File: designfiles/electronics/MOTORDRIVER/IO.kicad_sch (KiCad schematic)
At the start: 17 parts, among them J1 IMU1, J2 IMU2, J3 Conn_01x04_Socket, J4 Screw_Terminal_01x02, P1 USB_C_Plug_USB2.0, SW1 SW_DPST_x2

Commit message: made clearer foldernames and cleaned up
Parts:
- renumbered R115 to R42, R113 to R43
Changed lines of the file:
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@@
 		(dnp no)
 		(fields_autoplaced yes)
-		(property "Reference" "#PWR0330"
+		(property "Reference" "#PWR060"
 			(at 34.29 107.95 0)
 			(effects
@@
 			(project "motordriver"
 				(path "/c7634e88-16d1-45ec-9aac-9c841e03cf6d/38bc72d2-c2f6-4538-9c33-e1ab2a8ac987"
-					(reference "#PWR0330")
+					(reference "#PWR060")
 					(unit 1)
 				)
@@
 		(dnp no)
 		(fields_autoplaced yes)
-		(property "Reference" "#PWR065"
+		(property "Reference" "#PWR069"
 			(at 139.7 92.71 0)
 			(effects
@@
 			(project "motordriver"
 				(path "/c7634e88-16d1-45ec-9aac-9c841e03cf6d/38bc72d2-c2f6-4538-9c33-e1ab2a8ac987"
-					(reference "#PWR065")
+					(reference "#PWR069")
 					(unit 1)
 				)
@@
 		(dnp no)
 		(fields_autoplaced yes)
-		(property "Reference" "#PWR058"
+		(property "Reference" "#PWR062"
 			(at 72.39 102.87 0)
 			(effects
@@
 			(project "motordriver"
 				(path "/c7634e88-16d1-45ec-9aac-9c841e03cf6d/38bc72d2-c2f6-4538-9c33-e1ab2a8ac987"
-					(reference "#PWR058")
+					(reference "#PWR062")
 					(unit 1)
 				)
@@
 		(dnp no)
 		(fields_autoplaced yes)
-		(property "Reference" "#PWR0333"
+		(property "Reference" "#PWR063"
 			(at 81.28 99.06 0)
 			(effects
@@
 			(project "motordriver"
 				(path "/c7634e88-16d1-45ec-9aac-9c841e03cf6d/38bc72d2-c2f6-4538-9c33-e1ab2a8ac987"
-					(reference "#PWR0333")
+					(reference "#PWR063")
 					(unit 1)
 				)
@@
 		(dnp no)
 		(fields_autoplaced yes)
-		(property "Reference" "#PWR064"
+		(property "Reference" "#PWR068"
 			(at 149.86 90.17 0)
 			(effects
@@
 			(project "motordriver"
 				(path "/c7634e88-16d1-45ec-9aac-9c841e03cf6d/38bc72d2-c2f6-4538-9c33-e1ab2a8ac987"
-					(reference "#PWR064")
+					(reference "#PWR068")
 					(unit 1)
 				)
@@
 		(dnp no)
 		(fields_autoplaced yes)
-		(property "Reference" "#PWR067"
+		(property "Reference" "#PWR071"
 			(at 139.7 106.68 0)
 			(effects
@@
 			(project "motordriver"
 				(path "/c7634e88-16d1-45ec-9aac-9c841e03cf6d/38bc72d2-c2f6-4538-9c33-e1ab2a8ac987"
-					(reference "#PWR067")
+					(reference "#PWR071")
 					(unit 1)
 				)
@@
 		(on_board yes)
 		(dnp no)
-		(property "Reference" "#PWR062"
+		(property "Reference" "#PWR066"
 			(at 121.92 113.03 0)
 			(effects
@@
 			(project "motordriver"
 				(path "/c7634e88-16d1-45ec-9aac-9c841e03cf6d/38bc72d2-c2f6-4538-9c33-e1ab2a8ac987"
-					(reference "#PWR062")
+					(reference "#PWR066")
 					(unit 1)
 				)
@@
 		(dnp no)
 		(fields_autoplaced yes)
-		(property "Reference" "#PWR072"
+		(property "Reference" "#PWR076"
 			(at 193.04 128.27 0)
 			(effects
@@
 			(project "motordriver"
 				(path "/c7634e88-16d1-45ec-9aac-9c841e03cf6d/38bc72d2-c2f6-4538-9c33-e1ab2a8ac987"
-					(reference "#PWR072")
+					(reference "#PWR076")
 					(unit 1)
 				)
@@
 		(dnp no)
 		(fields_autoplaced yes)
-		(property "Reference" "#PWR071"
+		(property "Reference" "#PWR075"
 			(at 190.5 99.06 0)
 			(effects
@@
 			(project "motordriver"
 				(path "/c7634e88-16d1-45ec-9aac-9c841e03cf6d/38bc72d2-c2f6-4538-9c33-e1ab2a8ac987"
-					(reference "#PWR071")
+					(reference "#PWR075")
 					(unit 1)
 				)
@@
 		(dnp no)
 		(fields_autoplaced yes)
-		(property "Reference" "#PWR068"
+		(property "Reference" "#PWR072"
 			(at 149.86 118.11 0)
 			(effects
@@
 			(project "motordriver"
 				(path "/c7634e88-16d1-45ec-9aac-9c841e03cf6d/38bc72d2-c2f6-4538-9c33-e1ab2a8ac987"
-					(reference "#PWR068")
+					(reference "#PWR072")
 					(unit 1)
 				)
@@
 		(dnp no)
 		(fields_autoplaced yes)
-		(property "Reference" "#PWR069"
+		(property "Reference" "#PWR073"
 			(at 139.7 120.65 0)
 			(effects
@@
 			(project "motordriver"
 				(path "/c7634e88-16d1-45ec-9aac-9c841e03cf6d/38bc72d2-c2f6-4538-9c33-e1ab2a8ac987"
-					(reference "#PWR069")
+					(reference "#PWR073")
 					(unit 1)
 				)
@@
 		(dnp no)
 		(fields_autoplaced yes)
-		(property "Reference" "#PWR066"
+		(property "Reference" "#PWR070"
 			(at 149.86 104.14 0)
 			(effects
@@
 			(project "motordriver"
 				(path "/c7634e88-16d1-45ec-9aac-9c841e03cf6d/38bc72d2-c2f6-4538-9c33-e1ab2a8ac987"
-					(reference "#PWR066")
+					(reference "#PWR070")
 					(unit 1)
 				)
@@
 		(dnp no)
 		(fields_autoplaced yes)
-		(property "Reference" "R113"
+		(property "Reference" "R43"
 			(at 76.2 83.82 90)
 			(effects
@@
 			(project "motordriver"
 				(path "/c7634e88-16d1-45ec-9aac-9c841e03cf6d/38bc72d2-c2f6-4538-9c33-e1ab2a8ac987"
-					(reference "R113")
+					(reference "R43")
 					(unit 1)
 				)
@@
 		(dnp no)
 		(fields_autoplaced yes)
-		(property "Reference" "#PWR073"
+		(property "Reference" "#PWR078"
 			(at 242.57 96.52 0)
 			(effects
@@
 			(project "motordriver"
 				(path "/c7634e88-16d1-45ec-9aac-9c841e03cf6d/38bc72d2-c2f6-4538-9c33-e1ab2a8ac987"
-					(reference "#PWR073")
+					(reference "#PWR078")
 					(unit 1)
 				)
@@
 		(dnp no)
 		(fields_autoplaced yes)
-		(property "Reference" "#PWR074"
+		(property "Reference" "#PWR077"
 			(at 238.76 129.54 0)
 			(effects
@@
 			(project "motordriver"
 				(path "/c7634e88-16d1-45ec-9aac-9c841e03cf6d/38bc72d2-c2f6-4538-9c33-e1ab2a8ac987"
-					(reference "#PWR074")
+					(reference "#PWR077")
 					(unit 1)
 				)
@@
 		(on_board yes)
 		(dnp no)
-		(property "Reference" "#PWR063"
+		(property "Reference" "#PWR067"
 			(at 111.76 115.57 0)
 			(effects
@@
 			(project "motordriver"
 				(path "/c7634e88-16d1-45ec-9aac-9c841e03cf6d/38bc72d2-c2f6-4538-9c33-e1ab2a8ac987"
-					(reference "#PWR063")
+					(reference "#PWR067")
 					(unit 1)
 				)
@@
 		(dnp no)
 		(fields_autoplaced yes)
-		(property "Reference" "R115"
+		(property "Reference" "R42"
 			(at 27.94 88.9 90)
 			(effects
@@
 			(project "motordriver"
 				(path "/c7634e88-16d1-45ec-9aac-9c841e03cf6d/38bc72d2-c2f6-4538-9c33-e1ab2a8ac987"
-					(reference "R115")
+					(reference "R42")
 					(unit 1)
 				)
@@
 		(on_board yes)
 		(dnp no)
-		(property "Reference" "#PWR060"
+		(property "Reference" "#PWR064"
 			(at 121.92 86.36 0)
 			(effects
@@
 			(project "motordriver"
 				(path "/c7634e88-16d1-45ec-9aac-9c841e03cf6d/38bc72d2-c2f6-4538-9c33-e1ab2a8ac987"
-					(reference "#PWR060")
+					(reference "#PWR064")
 					(unit 1)
 				)
@@
 		(dnp no)
 		(fields_autoplaced yes)
-		(property "Reference" "#PWR0331"
+		(property "Reference" "#PWR061"
 			(at 34.29 110.49 0)
 			(effects
@@
 			(project "motordriver"
 				(path "/c7634e88-16d1-45ec-9aac-9c841e03cf6d/38bc72d2-c2f6-4538-9c33-e1ab2a8ac987"
-					(reference "#PWR0331")
+					(reference "#PWR061")
 					(unit 1)
 				)
@@
 		(dnp no)
 		(fields_autoplaced yes)
-		(property "Reference" "#PWR070"
+		(property "Reference" "#PWR074"
 			(at 176.53 93.98 0)
 			(effects
@@
 			(project "motordriver"
 				(path "/c7634e88-16d1-45ec-9aac-9c841e03cf6d/38bc72d2-c2f6-4538-9c33-e1ab2a8ac987"
-					(reference "#PWR070")
+					(reference "#PWR074")
 					(unit 1)
 				)
@@
 		(dnp no)
 		(fields_autoplaced yes)
-		(property "Reference" "#PWR0332"
+		(property "Reference" "#PWR058"
 			(at 22.86 104.14 0)
 			(effects
@@
 			(project "motordriver"
 				(path "/c7634e88-16d1-45ec-9aac-9c841e03cf6d/38bc72d2-c2f6-4538-9c33-e1ab2a8ac987"
-					(reference "#PWR0332")
+					(reference "#PWR058")
 					(unit 1)
 				)
@@
 		(on_board yes)
 		(dnp no)
-		(property "Reference" "#PWR061"
+		(property "Reference" "#PWR065"
 			(at 111.76 88.9 0)
 			(effects
@@
 			(project "motordriver"
 				(path "/c7634e88-16d1-45ec-9aac-9c841e03cf6d/38bc72d2-c2f6-4538-9c33-e1ab2a8ac987"
-					(reference "#PWR061")
-					(unit 1)
-				)
+					(reference "#PWR065")
+					(unit 1)
+				)

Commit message: removed backup files and found components for special resistors and diodes
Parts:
- renumbered R42 to R43, R43 to R44
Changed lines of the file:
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@@
 		(dnp no)
 		(fields_autoplaced yes)
-		(property "Reference" "R43"
+		(property "Reference" "R44"
 			(at 76.2 83.82 90)
 			(effects
@@
 			(project "motordriver"
 				(path "/c7634e88-16d1-45ec-9aac-9c841e03cf6d/38bc72d2-c2f6-4538-9c33-e1ab2a8ac987"
-					(reference "R43")
+					(reference "R44")
 					(unit 1)
 				)
@@
 		(dnp no)
 		(fields_autoplaced yes)
-		(property "Reference" "R42"
+		(property "Reference" "R43"
 			(at 27.94 88.9 90)
 			(effects
@@
 			(project "motordriver"
 				(path "/c7634e88-16d1-45ec-9aac-9c841e03cf6d/38bc72d2-c2f6-4538-9c33-e1ab2a8ac987"
-					(reference "R42")
-					(unit 1)
-				)
+					(reference "R43")
+					(unit 1)
+				)

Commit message: small tweaks
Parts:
- added SW1: SW_DPST_x2, Button_Switch_THT:SW_CK_JS202011AQN_DPDT_Angled, symbol Switch:SW_DPST_x2
- renumbered SW1 to SW2
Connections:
- new net RESETN: SW1.1 (A)
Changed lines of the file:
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@@
+		)
+	)
+	(hierarchical_label "RESETN"
+		(shape input)
+		(at 172.72 53.34 180)
+		(fields_autoplaced yes)
+		(effects
+			(font
+				(size 1.27 1.27)
+			)
+			(justify right)
 		)
 	)
@@
 	)
 	(symbol
+		(lib_id "Switch:SW_DPST_x2")
+		(at 177.8 53.34 0)
+		(unit 1)
+		(exclude_from_sim no)
+		(in_bom yes)
+		(on_board yes)
+		(dnp no)
+		(fields_autoplaced yes)
+		(property "Reference" "SW1"
+			(at 177.8 46.99 0)
+			(effects
+				(font
+					(size 1.27 1.27)
+				)
+			)
+		)
+		(property "Value" "SW_DPST_x2"
+			(at 177.8 49.53 0)
+			(effects
+				(font
+					(size 1.27 1.27)
+				)
+			)
+		)
+		(property "Footprint" "Button_Switch_THT:SW_CK_JS202011AQN_DPDT_Angled"
+			(at 177.8 53.34 0)
+			(effects
+				(font
+					(size 1.27 1.27)
+				)
+				(hide yes)
+			)
+		)
+		(property "Datasheet" "~"
+			(at 177.8 53.34 0)
+			(effects
+				(font
+					(size 1.27 1.27)
+				)
+				(hide yes)
+			)
+		)
+		(property "Description" "Single Pole Single Throw (SPST) switch, separate symbol"
+			(at 177.8 53.34 0)
+			(effects
+				(font
+					(size 1.27 1.27)
+				)
+				(hide yes)
+			)
+		)
+		(pin "3"
+		)
+		(pin "1"
+		)
+		(pin "4"
+		)
+		(pin "2"
+		)
+		(instances
+			(project "motordriver"
+				(path "/c7634e88-16d1-45ec-9aac-9c841e03cf6d/38bc72d2-c2f6-4538-9c33-e1ab2a8ac987"
+					(reference "SW1")
+					(unit 1)
+				)
+			)
+		)
+	)
+	(symbol
 		(lib_id "power:GND")
 		(at 81.28 92.71 0)
@@
 		(dnp no)
 		(fields_autoplaced yes)
-		(property "Reference" "SW1"
+		(property "Reference" "SW2"
 			(at 237.49 81.28 0)
 			(effects
@@
 			(project ""
 				(path "/c7634e88-16d1-45ec-9aac-9c841e03cf6d/38bc72d2-c2f6-4538-9c33-e1ab2a8ac987"
-					(reference "SW1")
-					(unit 1)
-				)
+					(reference "SW2")
+					(unit 1)
+				)

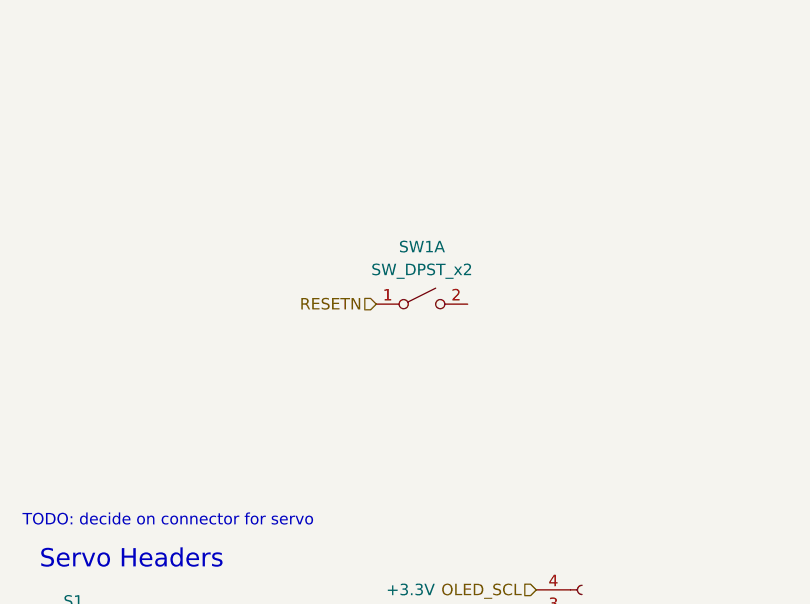
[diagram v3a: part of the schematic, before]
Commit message: tmc gpio pins fixed, spi db fixed, all mcu digital pins fixed, decoupled resetn
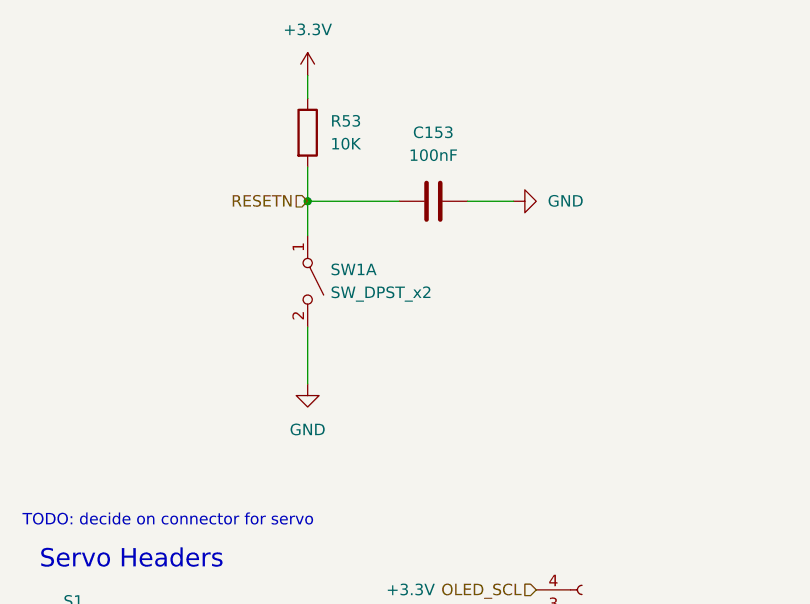
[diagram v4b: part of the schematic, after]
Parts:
- added C153: 100nF, symbol Device:C
- added R53: 10K, symbol Device:R
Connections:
- net +3.3V: now also R53.1
- net GND: now also SW1.2 (B), C153.2
- net RESETN: now also C153.1, R53.2
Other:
- moved on the sheet: SW1A

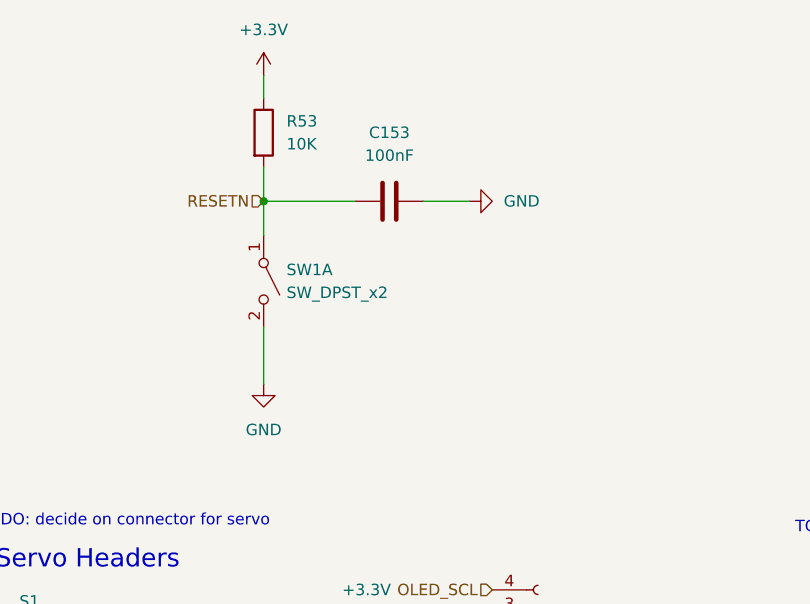
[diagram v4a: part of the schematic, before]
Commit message: added inductors
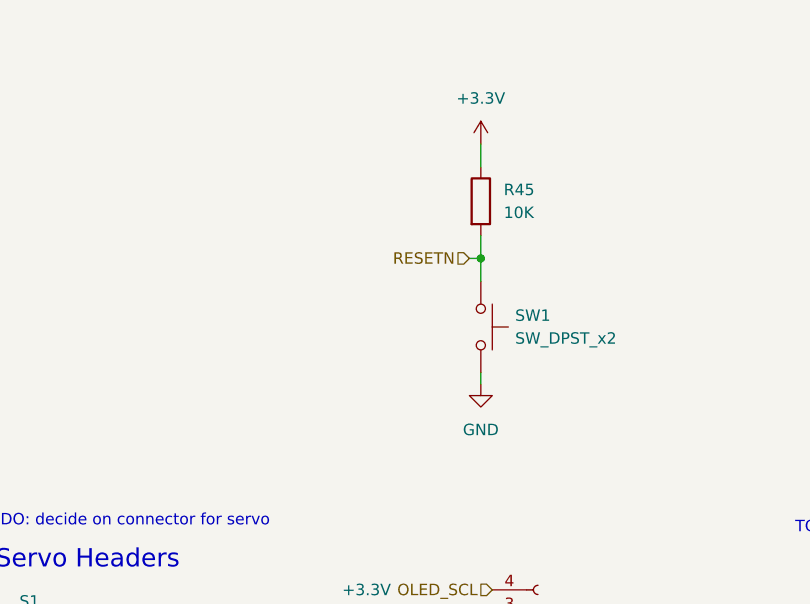
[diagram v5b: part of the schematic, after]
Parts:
- removed C153: 100nF, symbol Device:C
- J1, J2: footprint kuben-footprints:59453052110ECHLF -> 59453052110ECHLF
- P1: footprint kuben-footprints:USB4110GFA -> USB4110GFA
- R45: renamed from R53; footprint (none) -> Resistor_SMD:R_0603_1608Metric
- SW1: symbol Switch:SW_DPST_x2 -> Switch:SW_Push
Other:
- moved on the sheet: R45

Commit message: minor tweaks on schematic and started on the pcb layout, made good work
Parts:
- removed J4: Screw_Terminal_01x02, TerminalBlock:TerminalBlock_Altech_AK300-2_P5.00mm, symbol Connector:Screw_Terminal_01x02
- removed SW2: SW_DPST_x2, Button_Switch_THT:SW_CK_JS202011AQN_DPDT_Angled, symbol Switch:SW_DPST_x2
- added J4: XT60-M, kuben-footprints:AMASS_XT60-M, symbol XT60-M:XT60-M
- J1, J2: footprint 59453052110ECHLF -> kuben-footprints:59453052110ECHLF
- P1: footprint USB4110GFA -> kuben-footprints:USB4110GFA
- SW1: value SW_DPST_x2 -> PUSH; footprint Button_Switch_THT:SW_CK_JS202011AQN_DPDT_Angled -> Button_Switch_THT:SW_PUSH_6mm
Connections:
- net BATTVIN: now also J4.P (POS)
- net GND: now also J4.N (NEG)
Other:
- note removed: "TODO: Find right connector for battery"
- note removed: "TODO: decide on connector for servo"

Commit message: worked on PCB
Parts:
- added H1, H2, H3, H4: MountingHole, MountingHole:MountingHole_3.2mm_M3_DIN965_Pad, symbol Mechanical:MountingHole
- added J8: IMU2, kuben-footprints:59453052110ECHLF, symbol 59453-052110ECHLF:59453-052110ECHLF
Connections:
- net +3.3V: now also J8.2
- net GND: now also J8.1
- net INT1 IMU1 renamed INT_IMU1
- net INT1 IMU2 renamed INT_IMU2
- net SCL IMU1 renamed SCL_IMU1
- net SCL IMU2 renamed SCL_IMU2
- net SDA IMU1 renamed SDA_IMU1
- net SDA IMU2 renamed SDA_IMU2
- new net INT_IMU3: J8.5
- new net SCL_IMU3: J8.4
- new net SDA_IMU3: J8.3
- no-connect marks 10 -> 12
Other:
- moved on the sheet: J1, J2

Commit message: worked on PCB
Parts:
- removed H1, H2, H3, H4: MountingHole, MountingHole:MountingHole_3.2mm_M3_DIN965_Pad, symbol Mechanical:MountingHole
- removed J8: IMU2, kuben-footprints:59453052110ECHLF, symbol 59453-052110ECHLF:59453-052110ECHLF
- added H1, H2, H3, H4: MountingHole_Pad, MountingHole:MountingHole_3.2mm_M3_DIN965_Pad, symbol Mechanical:MountingHole_Pad
- renumbered J3 to J1, J1 to J3, J2 to J4, J4 to J6, R45 to R5, R44 to R72, R43 to R73, TP6 to TP2, TP2 to TP3, TP3 to TP4, TP4 to TP6
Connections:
- net GND: now also H1.1, H2.1, H3.1, H4.1
- no-connect marks 12 -> 10
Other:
- moved on the sheet: J3, J4
